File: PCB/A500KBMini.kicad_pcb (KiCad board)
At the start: 2 copper layers, 169.6 x 39.5 mm, 62 parts, among them J1 Conn_01x31, J2 USB_B_Micro, J3 Conn_02x03_Odd_Even, J4 Conn_01x08_Male, J5 Conn_01x02, Q1 MMBT3904, U1 IS32FL3237_DS, U2 AT90USB1287-AU, Y2 16 MHz

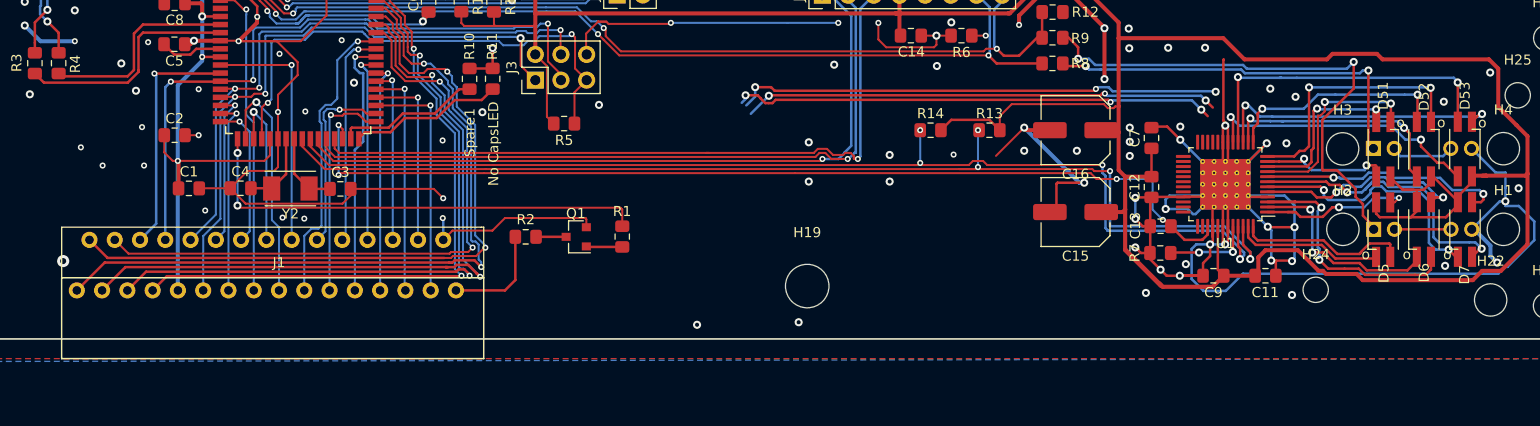
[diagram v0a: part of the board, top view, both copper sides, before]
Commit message: PCB update  - marked some unneeded components N/A  - changed LED footprints to fit PLCC LEDs better  - moved A500KBMini connector 0.5mm downwards
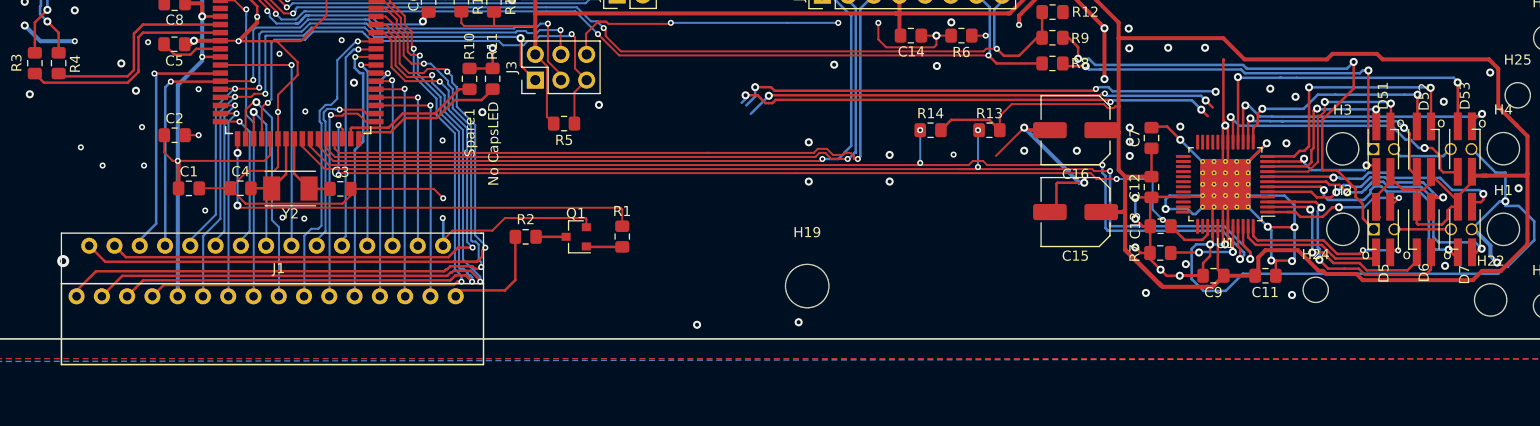
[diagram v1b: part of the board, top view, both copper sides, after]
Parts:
- C15: value 47uF SVP 47/10 -> not populated
- C16: value 47 uF SVP 47/10 -> not populated
- moved J1 0.58 mm to (342.8, 256.7)
- moved D3 0.06 mm to (456.0, 243.4)
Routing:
- net +5V: track 427.1 -> 429.7 mm
- net /F1G: track 17.0 -> 18.4 mm, vias 0 -> 2
- net /X3=5: track 67.4 -> 68.3 mm
- net /X2=7: track 65.5 -> 66.1 mm
